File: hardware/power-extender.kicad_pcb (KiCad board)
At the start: 2 copper layers, 59 parts, among them J1 Screw_Terminal_01x03, J2 Screw_Terminal_01x03, J3 Screw_Terminal_01x03, J4 Screw_Terminal_01x03, J5 Conn_01x04_Male, K1 SANYOU_SRD_Form_C, K2 SANYOU_SRD_Form_C, K3 SANYOU_SRD_Form_C, K4 SANYOU_SRD_Form_C, Q1 2N3904S-RTK/PS, Q2 2N3904S-RTK/PS, Q3 2N3904S-RTK/PS, Q4 2N3904S-RTK/PS, U1 PC817X2CSP9F, U10 ADS1115IDGS, U2 CC6902, U3 PC817X2CSP9F, U4 CC6902, U5 PC817X2CSP9F, U6 CC6902, U7 PC817X2CSP9F, U8 CC6902, U9 ADS1115IDGS

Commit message: Firnish schematic first version
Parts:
- added H1: MountingHole, MountingHole:MountingHole_3.2mm_M3, F.Cu at (190.6, 90.4)
- added H2: MountingHole, MountingHole:MountingHole_3.2mm_M3, F.Cu at (190.6, 98.3)
- added H3: MountingHole, MountingHole:MountingHole_3.2mm_M3, F.Cu at (198.6, 90.4)
- added H4: MountingHole, MountingHole:MountingHole_3.2mm_M3, F.Cu at (198.6, 98.3)
- added J6: AUX ANALOG, Connector_JST:JST_XH_B4B-XH-A_1x04_P2.50mm_Vertical, F.Cu at (151.6, 50.6)
- added J7: AUX DIGITAL, Connector_JST:JST_XH_B4B-XH-A_1x04_P2.50mm_Vertical, F.Cu at (147.0, 50.6)
- added J8: IFACE PASS, Connector_JST:JST_XH_B5B-XH-A_1x05_P2.50mm_Vertical, F.Cu at (108.0, 52.8)
- added Q5: BSS138, Package_TO_SOT_SMD:SOT-23, F.Cu at (156.2, 50.6)
- added Q6: BSS138, Package_TO_SOT_SMD:SOT-23, F.Cu at (138.7, 62.8)
- added R19: 1K, Resistor_SMD:R_0805_2012Metric, F.Cu at (143.1, 62.0)
- added R20: 10K, Resistor_SMD:R_0805_2012Metric, F.Cu at (129.9, 64.2)
- added R21: 10K, Resistor_SMD:R_0805_2012Metric, F.Cu at (138.7, 57.6)
- added U11: PCA9557PW, Package_SO:TSSOP-16_4.4x5mm_P0.65mm, F.Cu at (132.1, 59.4)
- C1, C10, C2, C3, C4, C5, C6, C7, C8, C9: footprint Capacitor_SMD:C_0201_0603Metric -> Capacitor_SMD:C_0805_2012Metric
- D1, D3, D5, D7: footprint LED_SMD:LED_0201_0603Metric -> LED_SMD:LED_0805_2012Metric
- J1, J2, J3, J4: value Screw_Terminal_01x03 -> LOAD
- J5: value Conn_01x04_Male -> IFACE RPI; footprint Connector_JST:JST_XH_B4B-XH-A_1x04_P2.50mm_Vertical -> Connector_JST:JST_XH_B5B-XH-A_1x05_P2.50mm_Vertical
- K1, K2, K3, K4: value SANYOU_SRD_Form_C -> SRD-05VDC-SL-C
- Q1, Q2, Q3, Q4: value 2N3904S-RTK/PS -> PMBT3904
- R1, R10, R4, R7: value 1K -> 200R; footprint Resistor_SMD:R_0201_0603Metric -> Resistor_SMD:R_0805_2012Metric
- R11, R12, R13, R14, R15, R16, R17, R18, R2, R3, R5, R6, R8, R9: footprint Resistor_SMD:R_0201_0603Metric -> Resistor_SMD:R_0805_2012Metric
- U2, U4, U6, U8: value CC6902 -> CC6902SO-10A; footprint CustomComponents:CC6902 -> CustomComponents:CC690XSO-XA
- moved U4 106.2 mm to (172.8, 52.7)
- moved U8 89.7 mm to (201.6, 52.7)
- moved U3 60.7 mm to (166.4, 55.3)
- moved R17 59.9 mm to (143.1, 65.0)
- moved R18 55.6 mm to (147.5, 62.0)
- moved J5 54.2 mm to (131.2, 51.7)
- moved U2 53.3 mm to (137.2, 74.1)
- moved U7 48.0 mm to (195.2, 55.3)
- moved U6 33.0 mm to (166.0, 74.1)
- moved U5 15.3 mm to (159.6, 76.6)
- moved U1 11.5 mm to (130.8, 76.6)
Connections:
- C10 pad 1: VCC -> +5V
- C2 pad 1: VCC -> +5V
- C4 pad 1: VCC -> +5V
- C6 pad 1: VCC -> +5V
- C8 pad 1: VCC -> +5V
- C9 pad 1: VCC -> +5V
- D1 pad 2: VCC -> Net-(D1-Pad2)
- D2 pad 1: VCC -> +5V
- D2 pad 2: Net-(D2-Pad2) -> Net-(D1-Pad1)
- D3 pad 2: VCC -> Net-(D3-Pad2)
- D4 pad 1: VCC -> +5V
- D4 pad 2: Net-(D4-Pad2) -> Net-(D3-Pad1)
- D5 pad 2: VCC -> Net-(D5-Pad2)
- D6 pad 1: VCC -> +5V
- D6 pad 2: Net-(D6-Pad2) -> Net-(D5-Pad1)
- D7 pad 2: VCC -> Net-(D7-Pad2)
- D8 pad 1: VCC -> +5V
- D8 pad 2: Net-(D8-Pad2) -> Net-(D7-Pad1)
- J5 pad 1: VCC -> +5V
- J5 pad 2: SDA -> +3V3
- J5 pad 3: SCL -> SDA3V3
- J5 pad 4: GND -> SCL3V3
- K1 pad 2: Net-(D2-Pad2) -> Net-(D1-Pad1)
- K1 pad 5: VCC -> +5V
- K2 pad 2: Net-(D4-Pad2) -> Net-(D3-Pad1)
- K2 pad 5: VCC -> +5V
- K3 pad 2: Net-(D6-Pad2) -> Net-(D5-Pad1)
- K3 pad 5: VCC -> +5V
- K4 pad 2: Net-(D8-Pad2) -> Net-(D7-Pad1)
- K4 pad 5: VCC -> +5V
- Q1 pad 3: Net-(D2-Pad2) -> Net-(D1-Pad1)
- Q2 pad 3: Net-(D4-Pad2) -> Net-(D3-Pad1)
- Q3 pad 3: Net-(D6-Pad2) -> Net-(D5-Pad1)
- Q4 pad 3: Net-(D8-Pad2) -> Net-(D7-Pad1)
- R1 pad 1: (no net) -> /Relay-A/TRIGGER
- R10 pad 1: (no net) -> /Relay-D/TRIGGER
- R11 pad 1: Net-(D7-Pad1) -> +5V
- R11 pad 2: Net-(D8-Pad2) -> Net-(D7-Pad2)
- R17 pad 1: VCC -> +3V3
- R17 pad 2: SDA -> SDA3V3
- R18 pad 1: VCC -> +3V3
- R18 pad 2: SCL -> SCL3V3
- R2 pad 1: Net-(D1-Pad1) -> +5V
- R2 pad 2: Net-(D2-Pad2) -> Net-(D1-Pad2)
- R4 pad 1: (no net) -> /Relay-B/TRIGGER
- R5 pad 1: Net-(D3-Pad1) -> +5V
- R5 pad 2: Net-(D4-Pad2) -> Net-(D3-Pad2)
- R7 pad 1: (no net) -> /Relay-C/TRIGGER
- R8 pad 1: Net-(D5-Pad1) -> +5V
- R8 pad 2: Net-(D6-Pad2) -> Net-(D5-Pad2)
- U1 pad 4: VCC -> +5V
- U10 pad 1: VCC -> +5V
- U10 pad 10: SCL -> SCL5V
- U10 pad 4: (no net) -> A0
- U10 pad 5: (no net) -> A1
- U10 pad 6: (no net) -> A2
- U10 pad 7: (no net) -> A3
- U10 pad 8: VCC -> +5V
- U10 pad 9: SDA -> SDA5V
- U2 pad 8: VCC -> +5V
- U3 pad 4: VCC -> +5V
- U4 pad 8: VCC -> +5V
- U5 pad 4: VCC -> +5V
- U6 pad 8: VCC -> +5V
- U7 pad 4: VCC -> +5V
- U8 pad 8: VCC -> +5V
- U9 pad 10: SCL -> SCL5V
- U9 pad 4: /Relay-D/VIOUT -> /Relay-A/VIOUT
- U9 pad 5: /Relay-C/VIOUT -> /Relay-B/VIOUT
- U9 pad 6: /Relay-B/VIOUT -> /Relay-C/VIOUT
- U9 pad 7: /Relay-A/VIOUT -> /Relay-D/VIOUT
- U9 pad 8: VCC -> +5V
- U9 pad 9: SDA -> SDA5V

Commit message: checkpoint commit
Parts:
- added FID1: Fiducial, Fiducial:Fiducial_1mm_Mask2mm, F.Cu at (182.4, 109.8)
- added FID2: Fiducial, Fiducial:Fiducial_1mm_Mask2mm, F.Cu at (186.9, 109.8)
- added FID3: Fiducial, Fiducial:Fiducial_1mm_Mask2mm, F.Cu at (191.6, 109.8)
- J1, J2, J3, J4: footprint TerminalBlock:TerminalBlock_Altech_AK300-3_P5.00mm -> TerminalBlock_Phoenix:TerminalBlock_Phoenix_MKDS-1,5-3_1x03_P5.00mm_Horizontal
- moved U4 143.7 mm to (55.2, 135.5), turned to 270 degrees
- moved C5 130.5 mm to (258.2, 140.6)
- moved D6 130.1 mm to (261.2, 154.2)
- moved U3 124.6 mm to (69.0, 133.0)
- moved C6 124.2 mm to (254.2, 129.2)
- moved R9 121.3 mm to (248.2, 137.4)
- moved U5 114.2 mm to (237.2, 160.4)
- moved R15 111.1 mm to (267.9, 107.4)
- moved U6 110.5 mm to (266.6, 119.8)
- moved D5 109.3 mm to (266.1, 129.6)
- moved R18 109.1 mm to (255.0, 80.8)
- moved R21 107.4 mm to (241.0, 90.0)
- moved R19 104.0 mm to (245.4, 81.0)
- moved Q3 100.7 mm to (226.8, 131.0)
- moved K3 100.1 mm to (224.3, 110.6)
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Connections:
- K1 pad 1: Net-(J1-Pad2) -> Net-(K1-Pad1)
- K2 pad 1: Net-(J2-Pad2) -> Net-(K2-Pad1)
- K3 pad 1: Net-(J3-Pad2) -> Net-(K3-Pad1)
- K4 pad 1: Net-(J4-Pad2) -> Net-(K4-Pad1)
- U10 pad 2: (no net) -> Net-(U10-Pad2)
- U2 pad 1: Net-(J1-Pad3) -> Net-(K1-Pad1)
- U2 pad 2: Net-(J1-Pad3) -> Net-(K1-Pad1)
- U2 pad 6: (no net) -> Net-(U2-Pad6)
- U4 pad 1: Net-(J2-Pad3) -> Net-(K2-Pad1)
- U4 pad 2: Net-(J2-Pad3) -> Net-(K2-Pad1)
- U4 pad 6: (no net) -> Net-(U4-Pad6)
- U6 pad 1: Net-(J3-Pad3) -> Net-(K3-Pad1)
- U6 pad 2: Net-(J3-Pad3) -> Net-(K3-Pad1)
- U6 pad 6: (no net) -> Net-(U6-Pad6)
- U8 pad 1: Net-(J4-Pad3) -> Net-(K4-Pad1)
- U8 pad 2: Net-(J4-Pad3) -> Net-(K4-Pad1)
- U8 pad 6: (no net) -> Net-(U8-Pad6)
- U9 pad 2: (no net) -> Net-(U9-Pad2)
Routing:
- net Net-(J2-Pad3): track 0.00 -> 35.2 mm
- net +5V: track 0.00 -> 31.5 mm
- net GND: track 0.00 -> 18.3 mm, vias 0 -> 3
- net Net-(K2-Pad1): track 0.00 -> 18.3 mm
- net Net-(D3-Pad1): track 0.00 -> 15.8 mm
- net Net-(Q2-Pad1): track 0.00 -> 9.20 mm
- net Net-(J2-Pad2): track 0.00 -> 9.16 mm
- net Net-(J2-Pad1): track 0.00 -> 6.33 mm
- net Net-(R14-Pad2): track 0.00 -> 5.67 mm
- net Net-(D3-Pad2): track 0.00 -> 4.52 mm
- net Net-(R4-Pad2): track 0.00 -> 3.73 mm
- net Net-(R6-Pad1): track 0.00 -> 3.52 mm
- net /Relay-B/VIOUT: track 0.00 -> 3.27 mm

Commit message: relay layout checkpoint
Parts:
- removed the C1 at (45.5, 103.5)
- removed the C2 at (45.5, 100.0)
- removed C3, C5, C7: 100P, Capacitor_SMD:C_0805_2012Metric
- removed C6, C8: 100N, Capacitor_SMD:C_0805_2012Metric
- removed D1, D5, D7: LED, LED_SMD:LED_0805_2012Metric
- removed D2, D6, D8: 1N4007F, Diode_SMD:D_SMA
- removed the J1 at (22.0, 79.0)
- removed the J3 at (249.4, 98.2)
- removed the J4 at (143.9, 126.9)
- removed K1, K3, K4: SRD-05VDC-SL-C, Relay_THT:Relay_SPDT_SANYOU_SRD_Series_Form_C
- removed the Q1 at (58.0, 78.0)
- removed Q3, Q4: PMBT3904, Package_TO_SOT_SMD:SOT-23
- removed the R1 at (89.2, 112.4)
- removed R10, R7, R8: 200R, Resistor_SMD:R_0805_2012Metric
- removed the R12 at (143.1, 151.2)
- removed the R13 at (41.0, 103.5)
- removed R15, R16: 100R, Resistor_SMD:R_0805_2012Metric
- removed the R2 at (86.0, 67.5)
- removed the R3 at (58.0, 82.5)
- removed the R4 at (68.5, 141.8)
- removed R9: 1K, Resistor_SMD:R_0805_2012Metric
- removed the U1 at (67.5, 86.0)
- removed the U2 at (40.1, 97.3)
- removed U5, U7: PC817X2CSP9F, CustomComponents:PC817X2CSP9F
- removed U6, U8: CC6902SO-10A, CustomComponents:CC690XSO-XA
- added C11: 100P, Capacitor_SMD:C_0805_2012Metric, F.Cu at (63.8, 140.2)
- added C21: 100P, Capacitor_SMD:C_0805_2012Metric, F.Cu at (63.8, 161.0)
- added C22: 100N, Capacitor_SMD:C_0805_2012Metric, F.Cu at (63.8, 154.8)
- added C31: 100P, Capacitor_SMD:C_0805_2012Metric, F.Cu at (94.2, 154.8)
- added C32: 100N, Capacitor_SMD:C_0805_2012Metric, F.Cu at (94.2, 161.0)
- added C41: 100P, Capacitor_SMD:C_0805_2012Metric, F.Cu at (94.2, 134.0)
- added C42: 100N, Capacitor_SMD:C_0805_2012Metric, F.Cu at (94.2, 140.2)
- added D21: LED, LED_SMD:LED_0805_2012Metric, F.Cu at (63.7, 171.0)
- added D22: 1N4007F, Diode_SMD:D_SMA, F.Cu at (63.8, 177.0)
- added D31: LED, LED_SMD:LED_0805_2012Metric, F.Cu at (94.2, 175.0)
- added D32: 1N4007F, Diode_SMD:D_SMA, F.Cu at (94.2, 169.0)
- added D41: LED, LED_SMD:LED_0805_2012Metric, F.Cu at (94.3, 124.0)
- added D42: 1N4007F, Diode_SMD:D_SMA, F.Cu at (94.2, 118.0)
- added J21: LOAD, TerminalBlock_Phoenix:TerminalBlock_Phoenix_MKDS-1,5-3_1x03_P5.00mm_Horizontal, F.Cu at (44.0, 151.0)
- added J31: LOAD, TerminalBlock_Phoenix:TerminalBlock_Phoenix_MKDS-1,5-3_1x03_P5.00mm_Horizontal, F.Cu at (114.0, 161.0)
- added J41: LOAD, TerminalBlock_Phoenix:TerminalBlock_Phoenix_MKDS-1,5-3_1x03_P5.00mm_Horizontal, F.Cu at (114.0, 144.0)
- added K21: SRD-05VDC-SL-C, Relay_THT:Relay_SPDT_SANYOU_SRD_Series_Form_C, F.Cu at (57.4, 173.0)
- added K31: SRD-05VDC-SL-C, Relay_THT:Relay_SPDT_SANYOU_SRD_Series_Form_C, F.Cu at (100.7, 173.0)
- added K41: SRD-05VDC-SL-C, Relay_THT:Relay_SPDT_SANYOU_SRD_Series_Form_C, F.Cu at (100.7, 122.0)
- added Q21: PMBT3904, Package_TO_SOT_SMD:SOT-23, F.Cu at (63.7, 167.0)
- added Q31: PMBT3904, Package_TO_SOT_SMD:SOT-23, F.Cu at (94.2, 179.0)
- added Q41: PMBT3904, Package_TO_SOT_SMD:SOT-23, F.Cu at (94.3, 128.0)
- added R21: 200R, Resistor_SMD:R_0805_2012Metric, F.Cu at (71.2, 152.7)
- added R22: 200R, Resistor_SMD:R_0805_2012Metric, F.Cu at (69.0, 174.0)
- added R23: 1K, Resistor_SMD:R_0805_2012Metric, F.Cu at (67.8, 170.0)
- added R24: 100R, Resistor_SMD:R_0805_2012Metric, F.Cu at (63.7, 157.8)
- added R31: 200R, Resistor_SMD:R_0805_2012Metric, F.Cu at (89.4, 153.8)
- added R32: 200R, Resistor_SMD:R_0805_2012Metric, F.Cu at (90.5, 171.5)
- added R33: 1K, Resistor_SMD:R_0805_2012Metric, F.Cu at (87.8, 171.5)
- added R34: 100R, Resistor_SMD:R_0805_2012Metric, F.Cu at (94.2, 158.0)
- added R41: 200R, Resistor_SMD:R_0805_2012Metric, F.Cu at (86.8, 142.3)
- added R42: 200R, Resistor_SMD:R_0805_2012Metric, F.Cu at (89.0, 121.0)
- added R43: 1K, Resistor_SMD:R_0805_2012Metric, F.Cu at (90.2, 125.0)
- added R44: 100R, Resistor_SMD:R_0805_2012Metric, F.Cu at (94.3, 137.2)
- added U21: PC817X2CSP9F, CustomComponents:PC817X2CSP9F, F.Cu at (69.0, 161.0)
- added U22: CC6902SO-10A, CustomComponents:CC690XSO-XA, F.Cu at (55.2, 159.5)
- added U31: PC817X2CSP9F, CustomComponents:PC817X2CSP9F, F.Cu at (89.0, 162.0)
- added U32: CC6902SO-10A, CustomComponents:CC690XSO-XA, F.Cu at (102.8, 159.5)
- added U41: PC817X2CSP9F, CustomComponents:PC817X2CSP9F, F.Cu at (89.0, 134.0)
- added U42: CC6902SO-10A, CustomComponents:CC690XSO-XA, F.Cu at (102.8, 135.5)
- moved FID2 165.6 mm to (36.0, 178.0)
- moved H2 153.9 mm to (36.0, 184.0)
- moved H1 143.5 mm to (36.0, 111.0)
- moved FID1 140.4 mm to (42.0, 111.0)
- moved U2 120.3 mm to (233.8, 53.8)
- moved H3 91.5 mm to (122.0, 184.0), turned to 180 degrees
- moved Q1 81.6 mm to (215.8, 39.8)
- moved FID3 70.0 mm to (122.0, 117.0)
- moved H4 67.3 mm to (122.0, 111.0), turned to 180 degrees
- moved U1 66.8 mm to (222.2, 46.5)
- moved C1 60.7 mm to (213.4, 47.5)
- moved R11 48.8 mm to (68.6, 141.2), turned to 180 degrees
- moved C2 39.1 mm to (212.0, 58.2)
- moved R4 35.5 mm to (224.3, 70.8)
- moved U3 28.9 mm to (214.0, 67.2)
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- renumbered C9 to C1, C4 to C12, C10 to C2, D3 to D11, D4 to D12, J5 to J1, J2 to J11, J8 to J2, J6 to J3, J7 to J4, K2 to K11, Q5 to Q1, Q2 to Q11, Q6 to Q2, R19 to R1, R5 to R12, R6 to R13, R17 to R2, R18 to R3, R20 to R4, R21 to R5, U9 to U1, U3 to U11, U4 to U12, U11 to U2, U10 to U3
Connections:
- R11 pad 1: +5V -> /Relay-A/TRIGGER
- R11 pad 2: Net-(D7-Pad2) -> Net-(R11-Pad2)
- R14 pad 1: /Relay-B/VIOUT -> /Relay-A/VIOUT
- U11 pad 1: Net-(R4-Pad2) -> Net-(R11-Pad2)
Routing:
- net +5V: track 31.5 -> 218.9 mm, vias 0 -> 6
- net GND: track 18.3 -> 73.6 mm, vias 3 -> 12
- net Net-(J21-Pad1): track 0.00 -> 35.2 mm
- net Net-(J31-Pad3): track 0.00 -> 35.2 mm
- net Net-(J41-Pad1): track 0.00 -> 35.2 mm
- net Net-(K41-Pad1): track 0.00 -> 18.3 mm
- net Net-(K31-Pad1): track 0.00 -> 18.3 mm
- net Net-(K21-Pad1): track 0.00 -> 18.3 mm
- net /Relay-D/VIOUT: track 0.00 -> 15.9 mm
- net Net-(D21-Pad1): track 0.00 -> 15.8 mm
- net Net-(D41-Pad1): track 0.00 -> 15.8 mm
- net Net-(D31-Pad1): track 0.00 -> 15.8 mm
- net /Relay-C/VIOUT: track 0.00 -> 13.1 mm
- net /Relay-A/VIOUT: track 0.00 -> 13.1 mm
- net /Relay-B/VIOUT: track 3.27 -> 15.9 mm
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
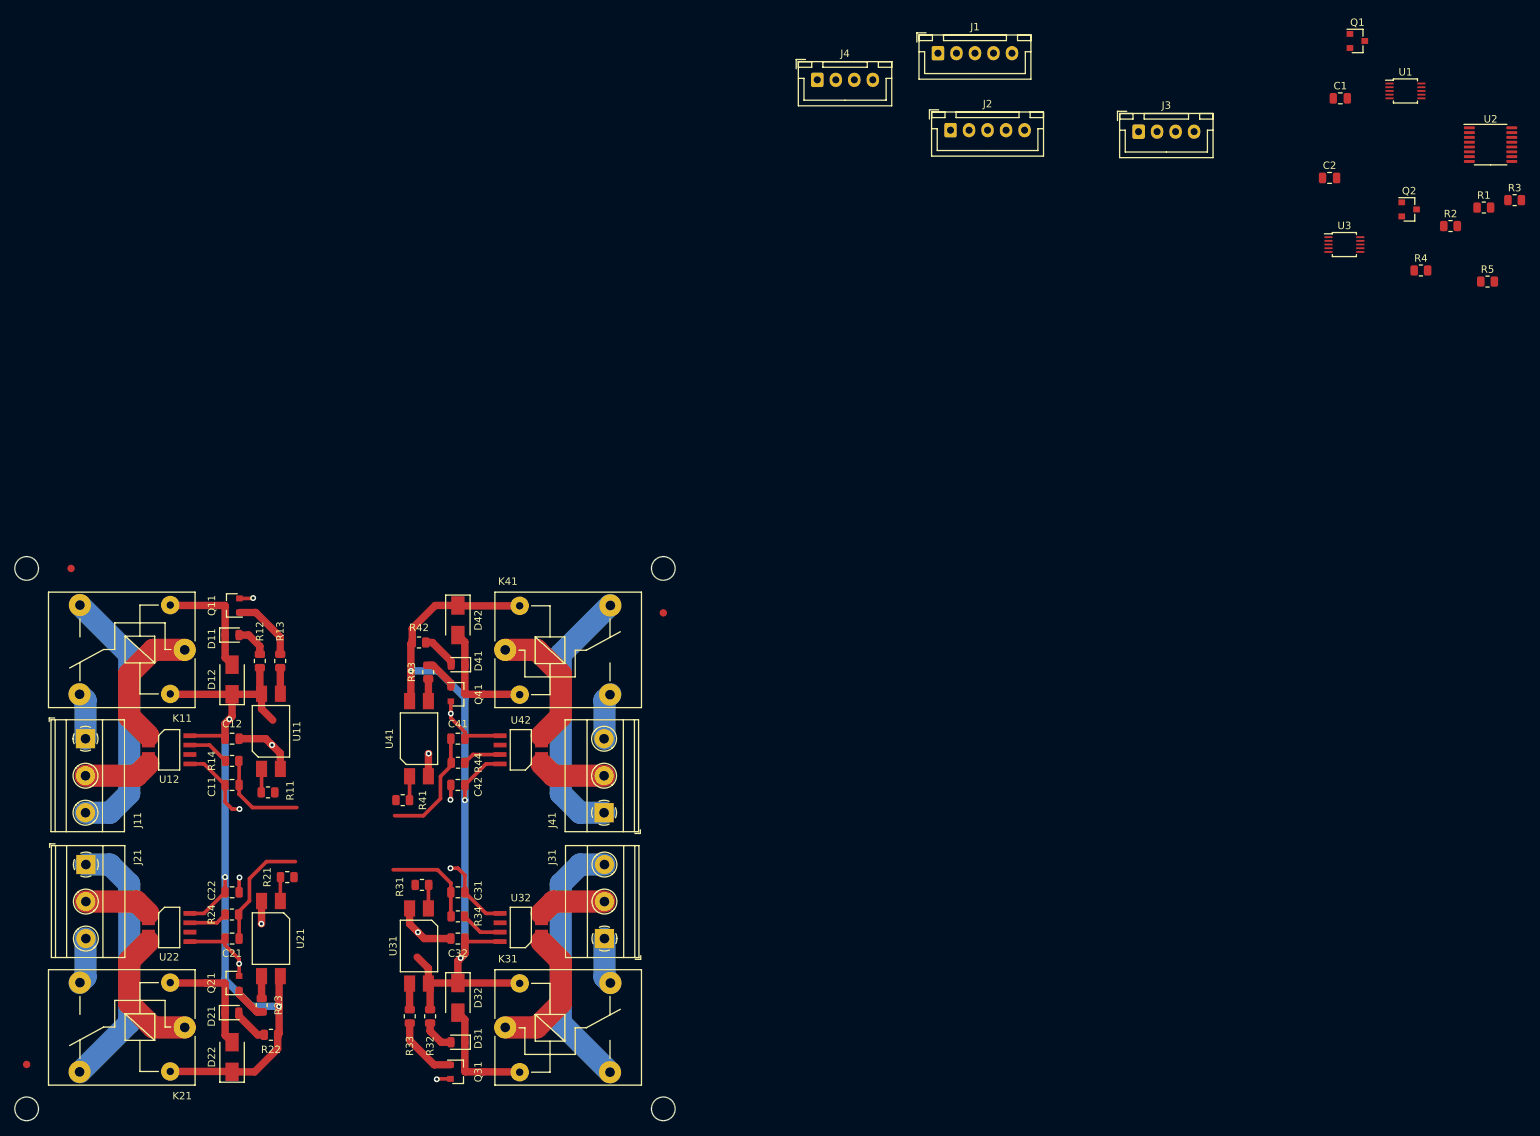
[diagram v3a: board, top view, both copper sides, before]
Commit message: traces done
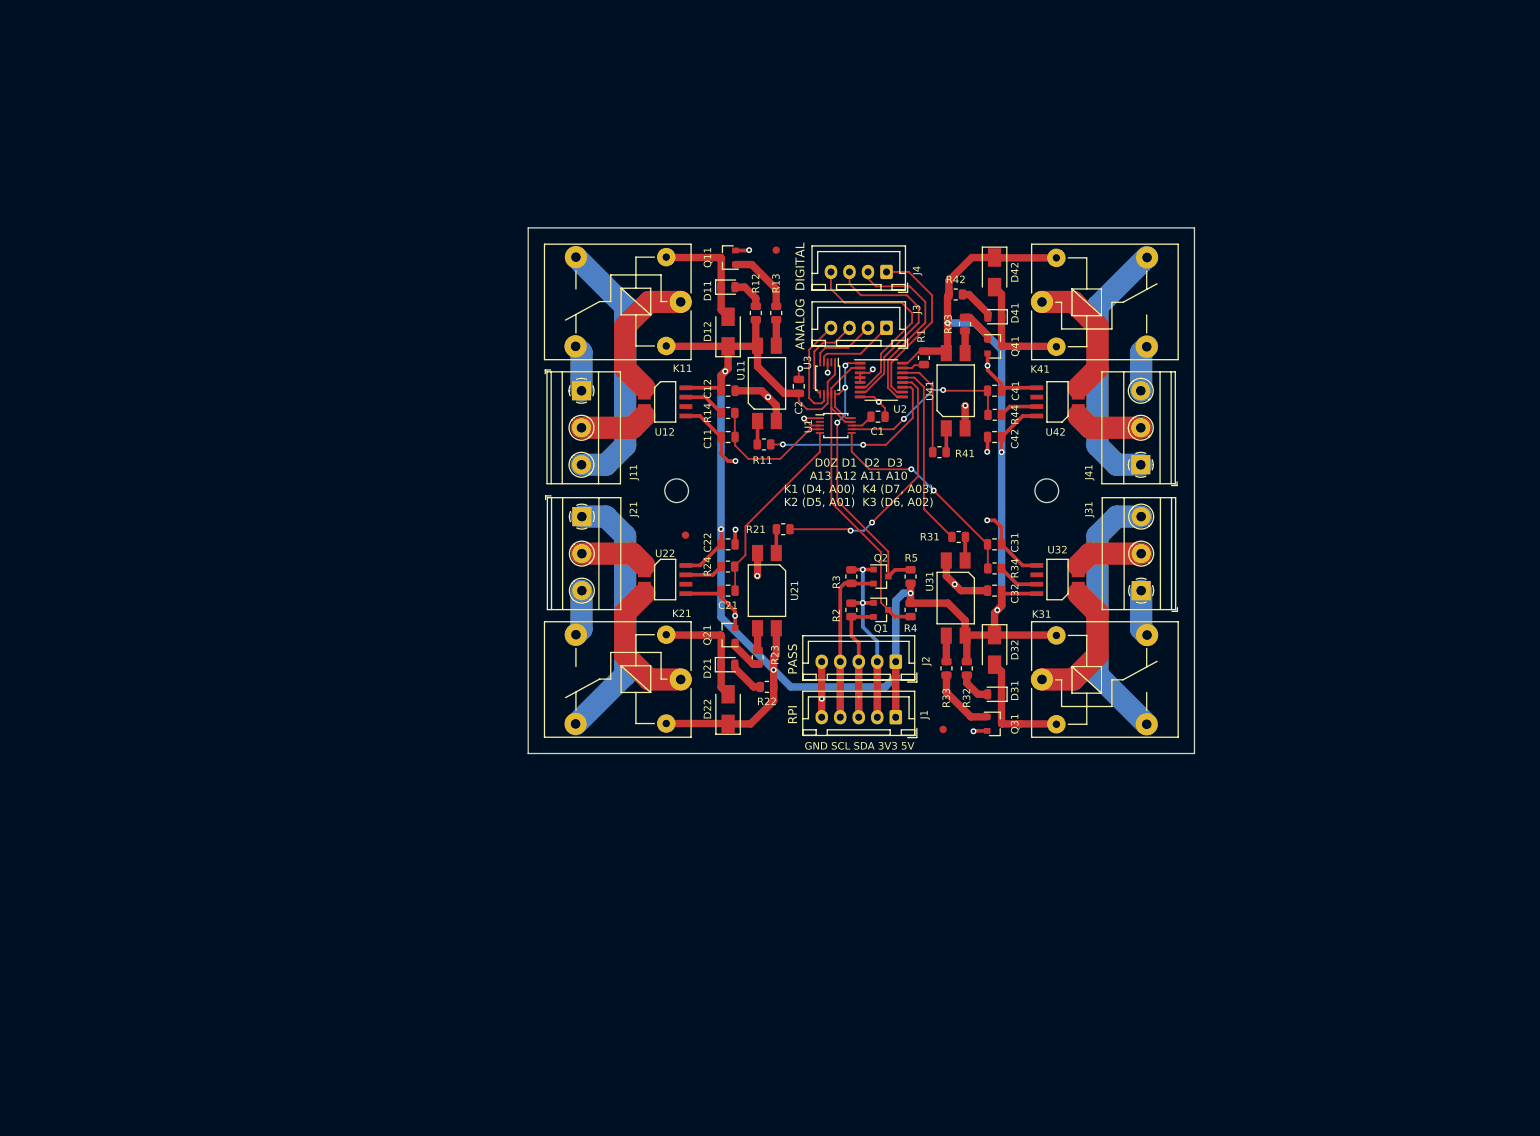
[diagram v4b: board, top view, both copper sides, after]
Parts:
- removed H3, H4: MountingHole, MountingHole:MountingHole_3.2mm_M3
- moved H2 161.1 mm to (173.8, 100.5)
- moved FID2 114.2 mm to (125.0, 106.5)
- moved FID1 104.5 mm to (137.2, 68.0)
- moved R3 103.0 mm to (147.4, 112.1), turned to 270 degrees
- moved Q1 100.2 mm to (151.4, 116.6)
- moved R2 96.1 mm to (147.4, 116.6), turned to 270 degrees
- moved J1 89.9 mm to (153.4, 131.1), turned to 180 degrees
- moved U1 89.2 mm to (145.3, 91.7)
- moved H1 88.4 mm to (123.8, 100.5)
- moved U2 88.2 mm to (151.4, 85.5)
- moved R5 87.5 mm to (155.4, 112.1), turned to 90 degrees
- moved Q2 86.9 mm to (151.4, 112.1)
- moved R41 86.4 mm to (159.3, 95.3)
- moved J31 86.4 mm to (186.6, 114.0)
- moved Q41 86.4 mm to (166.8, 81.0)
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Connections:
- J4 pad 1: D0Z -> D3
- J4 pad 2: D1 -> D2
- J4 pad 3: D2 -> D1
- J4 pad 4: D3 -> D0Z
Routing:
- net +5V: track 218.9 -> 292.8 mm, vias 6 -> 7
- net SDA5V: track 0.00 -> 45.1 mm
- net SCL5V: track 0.00 -> 43.7 mm, vias 0 -> 3
- net /Relay-B/TRIGGER: track 0.00 -> 34.7 mm, vias 0 -> 2
- net D0Z: track 0.00 -> 28.0 mm
- net D1: track 0.00 -> 27.4 mm
- net +3V3: track 0.00 -> 26.8 mm, vias 0 -> 2
- net D2: track 0.00 -> 26.1 mm
- net /Relay-A/TRIGGER: track 0.00 -> 26.1 mm, vias 0 -> 2
- net /Relay-C/TRIGGER: track 0.00 -> 25.2 mm
- net D3: track 0.00 -> 23.9 mm
- net GND: track 73.6 -> 97.1 mm, vias 12 -> 18
- net SCL3V3: track 0.00 -> 22.3 mm
- net SDA3V3: track 0.00 -> 17.0 mm
- net /Relay-C/VIOUT: track 13.1 -> 29.3 mm, vias 0 -> 2
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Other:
- board outline added: 90 x 71 mm
- board text added: "ANALOG"
- board text added: "D0Z D1 D2 D3 A13 A12 A11 A10 K1 (D4, A00) K4 (D7, A03) K2 (D5, A01) K3 (D6, A02)"
- board text added: "DIGITAL"
- board text added: "GND SCL SDA 3V3 5V"
- board text added: "PASS"
- board text added: "RPI"

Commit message: first verion of layout done
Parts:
- added REF**: OSHW-Logo2_14.6x12mm_SilkScreen, Symbol:OSHW-Logo2_14.6x12mm_SilkScreen, B.Cu at (148.5, 100.5)
- moved FID3 1.00 mm to (159.8, 131.8)
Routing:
- added copper zone on B.Cu, net GND
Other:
- outline, holes or cut-outs redrawn
- board text added: "D0Z D1 D2 D3 A13 A12 A11 A10 K1 (D4, +A00) K4 (D7, +A03) K2 (D5, -A01) K3 (D6, -A02)"
- board text added: "I2C: 3V3 RELAY MAX: 10A"
- board text added: "NC COM NO"
- board text added: "Power Extender REV1 CHRZ 2021"
- board text added: "https://github.com/StarGate01/power-extender"
- board text removed: "D0Z D1 D2 D3 A13 A12 A11 A10 K1 (D4, A00) K4 (D7, A03) K2 (D5, A01) K3 (D6, A02)"
